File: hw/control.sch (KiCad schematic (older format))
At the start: 13 parts, among them U201 XTAL_OSC, U202 74HC74, U203 74HC161, U204 74HC574, U205 27C64, U206 27C64, U207 27C64, U208 27C64, U209 74HCT574, U210 74HCT574, U211 74HCT574, U212 74HCT574, U213 74LS08

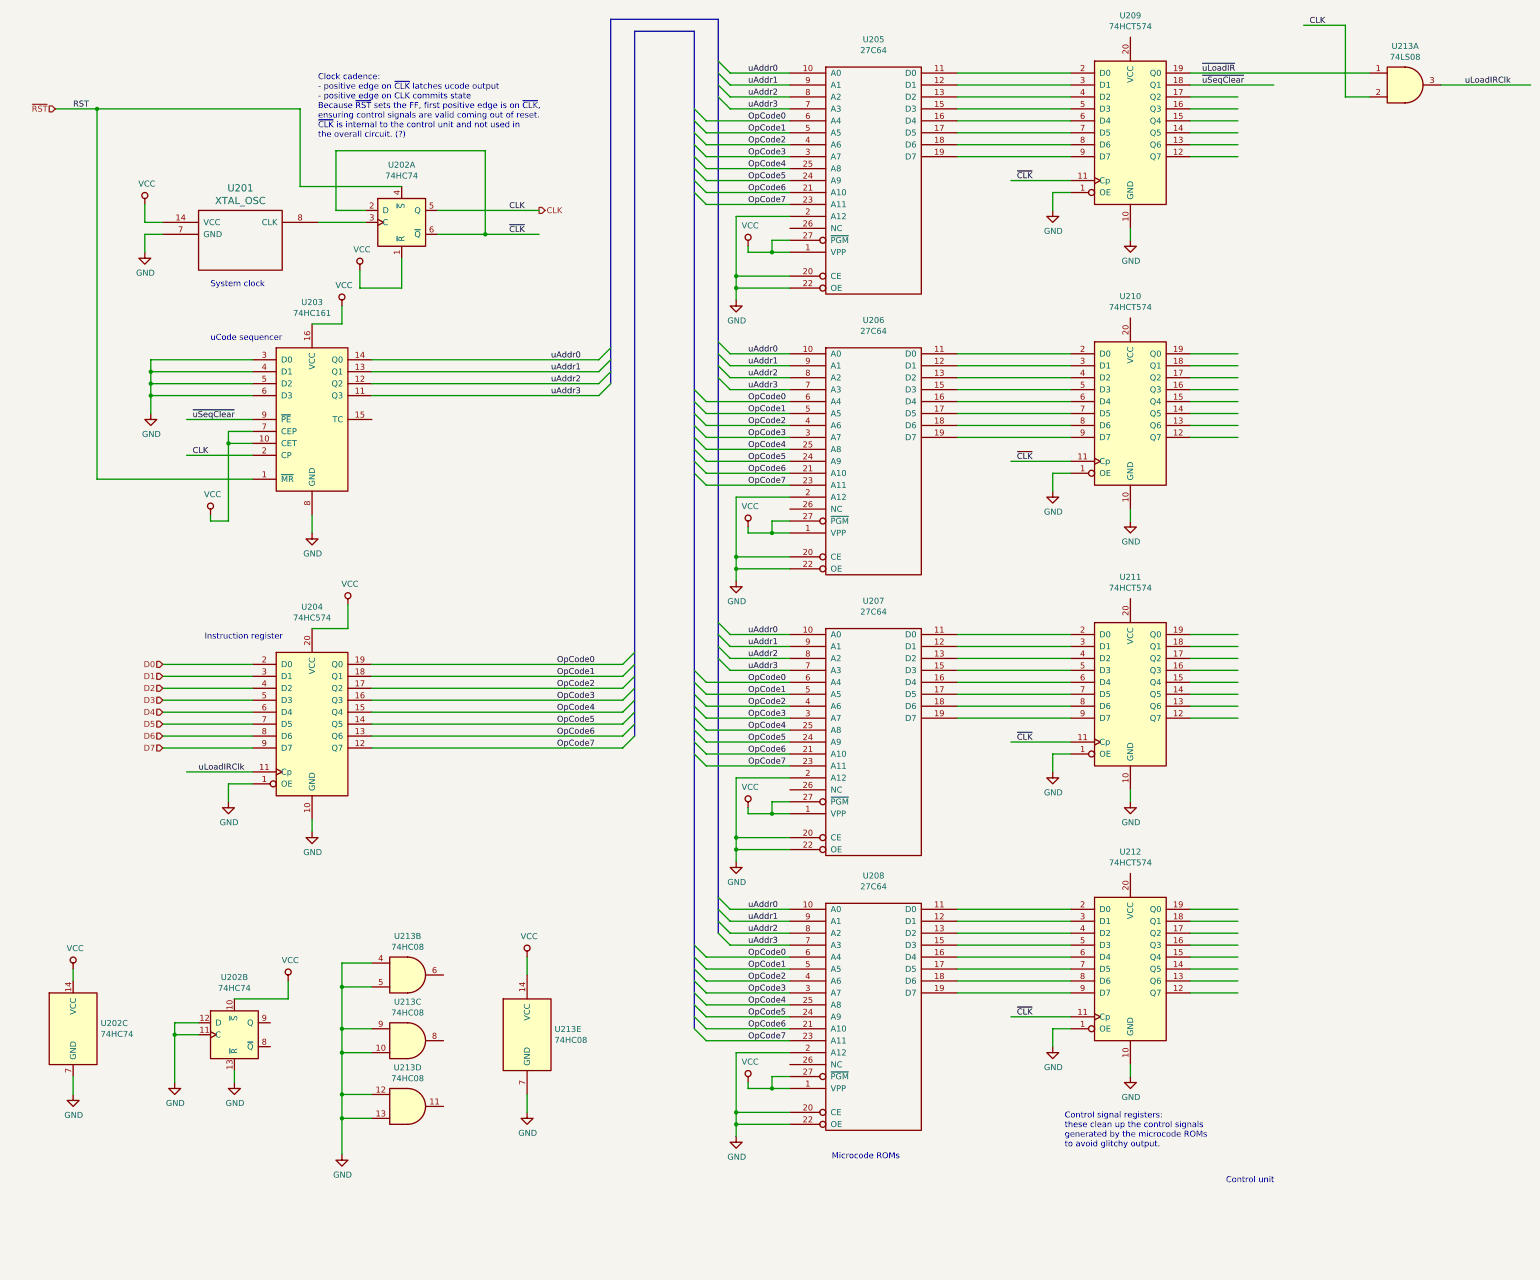
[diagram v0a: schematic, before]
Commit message: generation of -R/-W signals for mem transactions
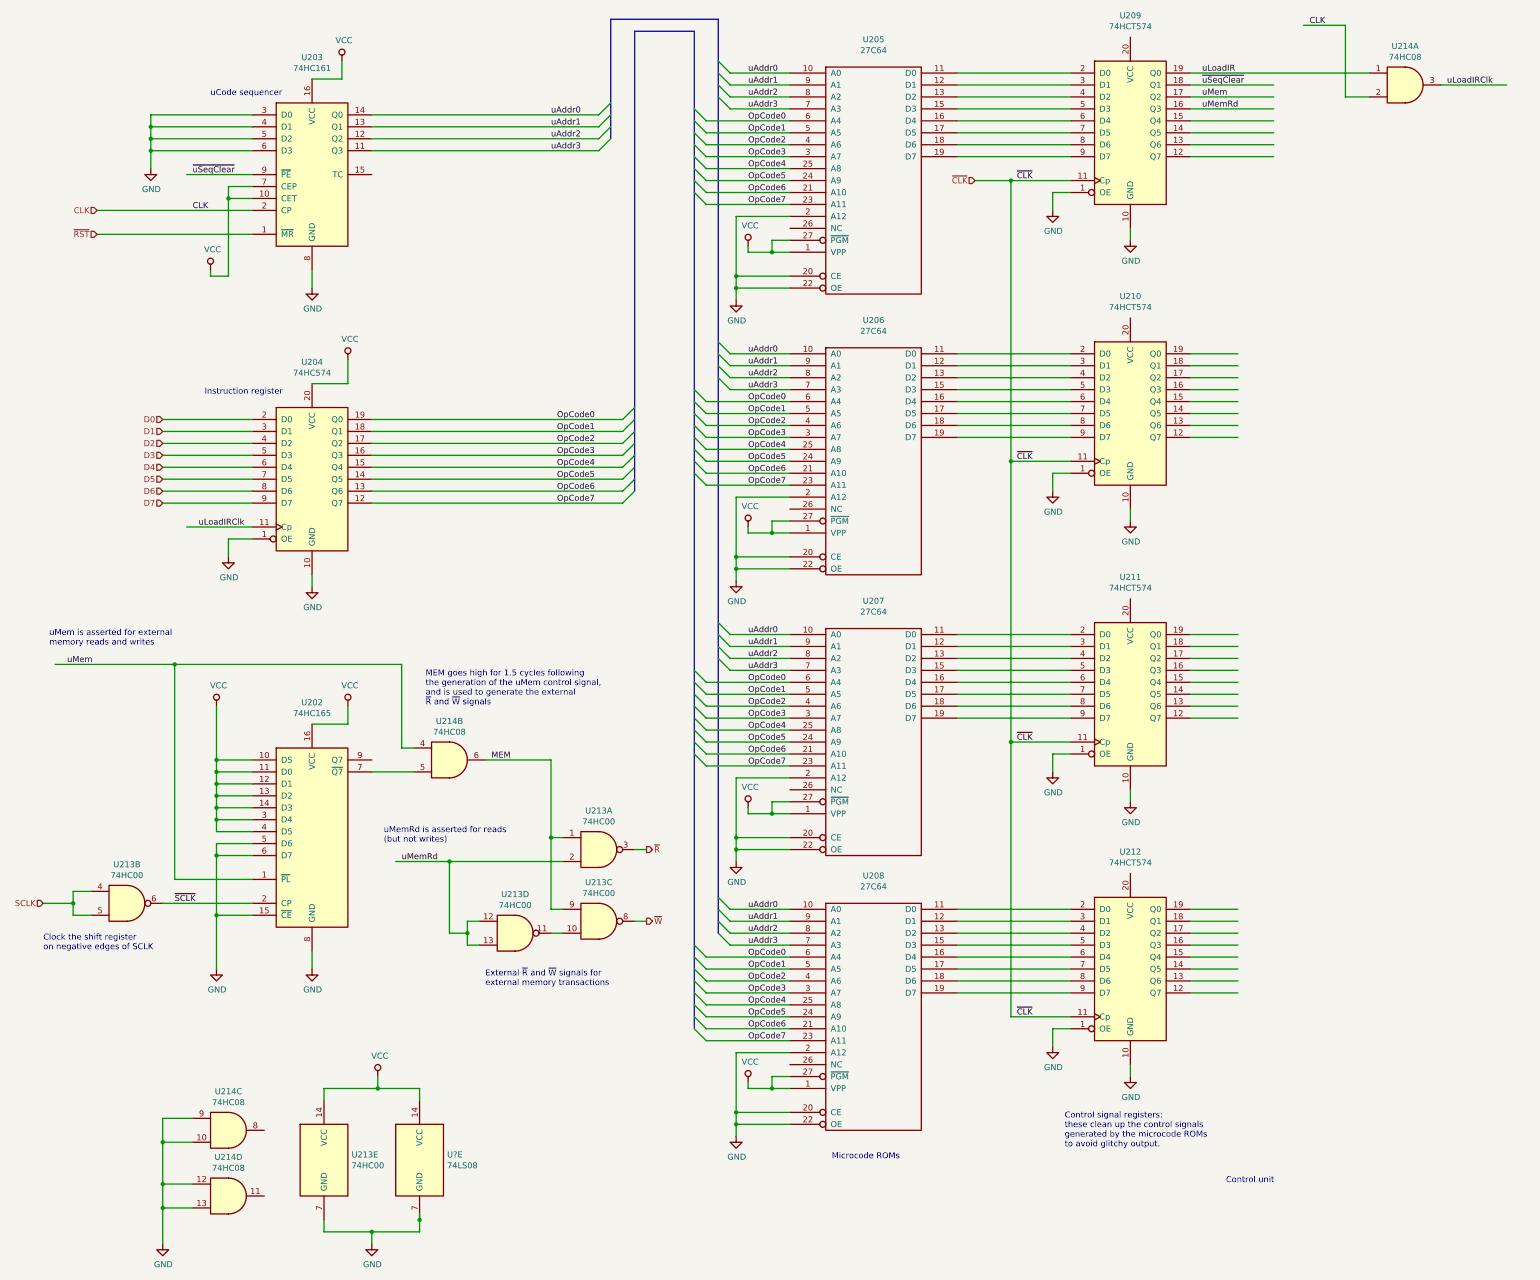
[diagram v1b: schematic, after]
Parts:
- removed U201: XTAL_OSC, symbol ya68k:XTAL_OSC
- removed U202: 74HC74, symbol 74xx:74HC74
- removed U213: 74LS08, symbol 74xx:74LS08
- added U202: 74HC165, symbol 74xx:74LS165
- added U213: 74HC00, symbol 74xx:74HC00
- added U214: 74HC08, symbol 74xx:74LS08
- added U?: 74LS08, symbol 74xx:74LS08
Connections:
- net labels added: MEM, SCLK, uLoadIR, uMem, uMemRd, ~R, ~SCLK~, ~W
- net labels removed: RST, ~uLoadIR
- wire segments 265 -> 297
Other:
- note added: "Clock the shift register\non negative edges of SCLK"
- note added: "External ~R~ and ~W~ signals for\nexternal memory transactions"
- note added: "MEM goes high for 1.5 cycles following\nthe generation of the uMem control signal,\nand is used to generate the external\n~R~ and ~W~ signals"
- note added: "uMem is asserted for external\nmemory reads and writes"
- note added: "uMemRd is asserted for reads\n(but not writes)"
- note removed: "Clock cadence:\n- positive edge on ~CLK~ latches ucode output\n- positive edge on CLK commits state\nBecause ~RST~ sets the FF, first positive edge is on ~CLK~,\nensuring control signals are valid coming out of reset.\n~CLK~ is internal to the control unit and not used in\nthe overall circuit. (?)"
- note removed: "System clock"
- moved on the sheet: U203, U204

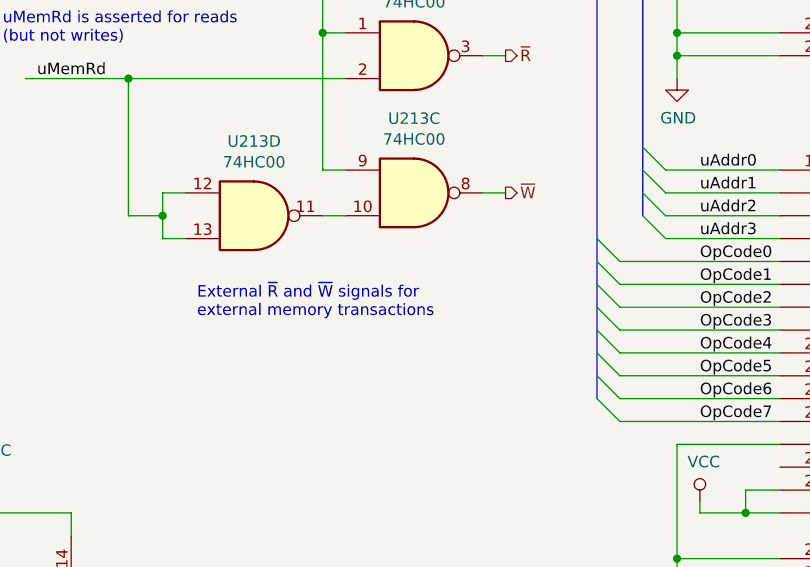
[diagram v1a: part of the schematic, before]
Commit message: minor tweaks, added sheet pins on main schematic?
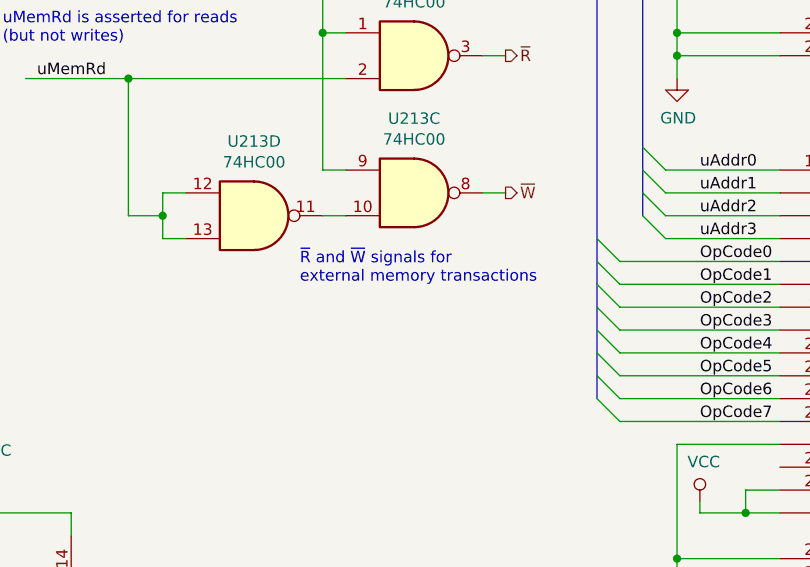
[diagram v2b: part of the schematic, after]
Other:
- note added: "~R~ and ~W~ signals for\nexternal memory transactions"
- note removed: "External ~R~ and ~W~ signals for\nexternal memory transactions"
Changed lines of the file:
@@
 $Descr User 15400 11900
 encoding utf-8
-Sheet 3 5
+Sheet 3 4
 Title ""
 Date ""
@@
 	9000 8950 9000 6650
 Connection ~ 9000 6650
-Text Notes 4600 8700 0    50   ~ 0
-External ~R~ and ~W~ signals for\nexternal memory transactions
+Text Notes 5050 8550 0    50   ~ 0
+~R~ and ~W~ signals for\nexternal memory transactions
 Wire Bus Line
 	5650 600  5650 1600
